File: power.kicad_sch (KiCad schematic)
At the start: 96 parts, among them Q5 NX138BKWX

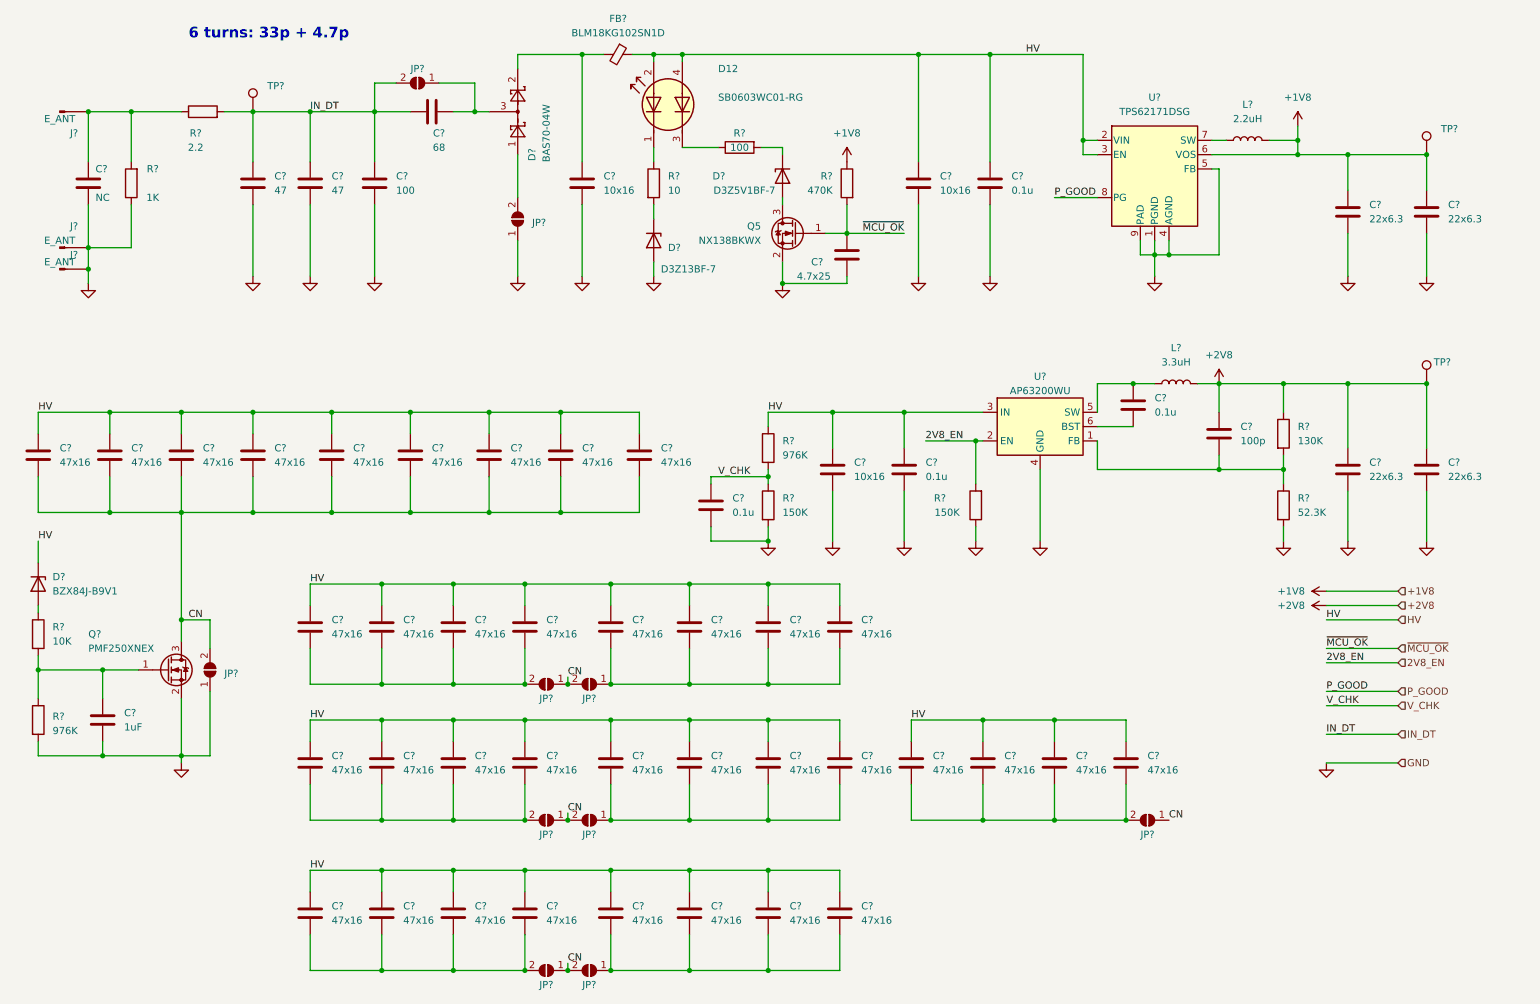
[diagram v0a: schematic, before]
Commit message: G2 revision
G2 revision = Kampela development kit

Features:
- electronics is more stable and reliable
- better power harvesting efficiency
- fixed a touchscreen instability with powerful NFC transmitters
- mechanical layout improved for low-volume productions for a devkit batch
- NFC coil placed closer to the phone antenna. The coil parameters are optimized based on a mathematical model of the NFS harvester circuit.
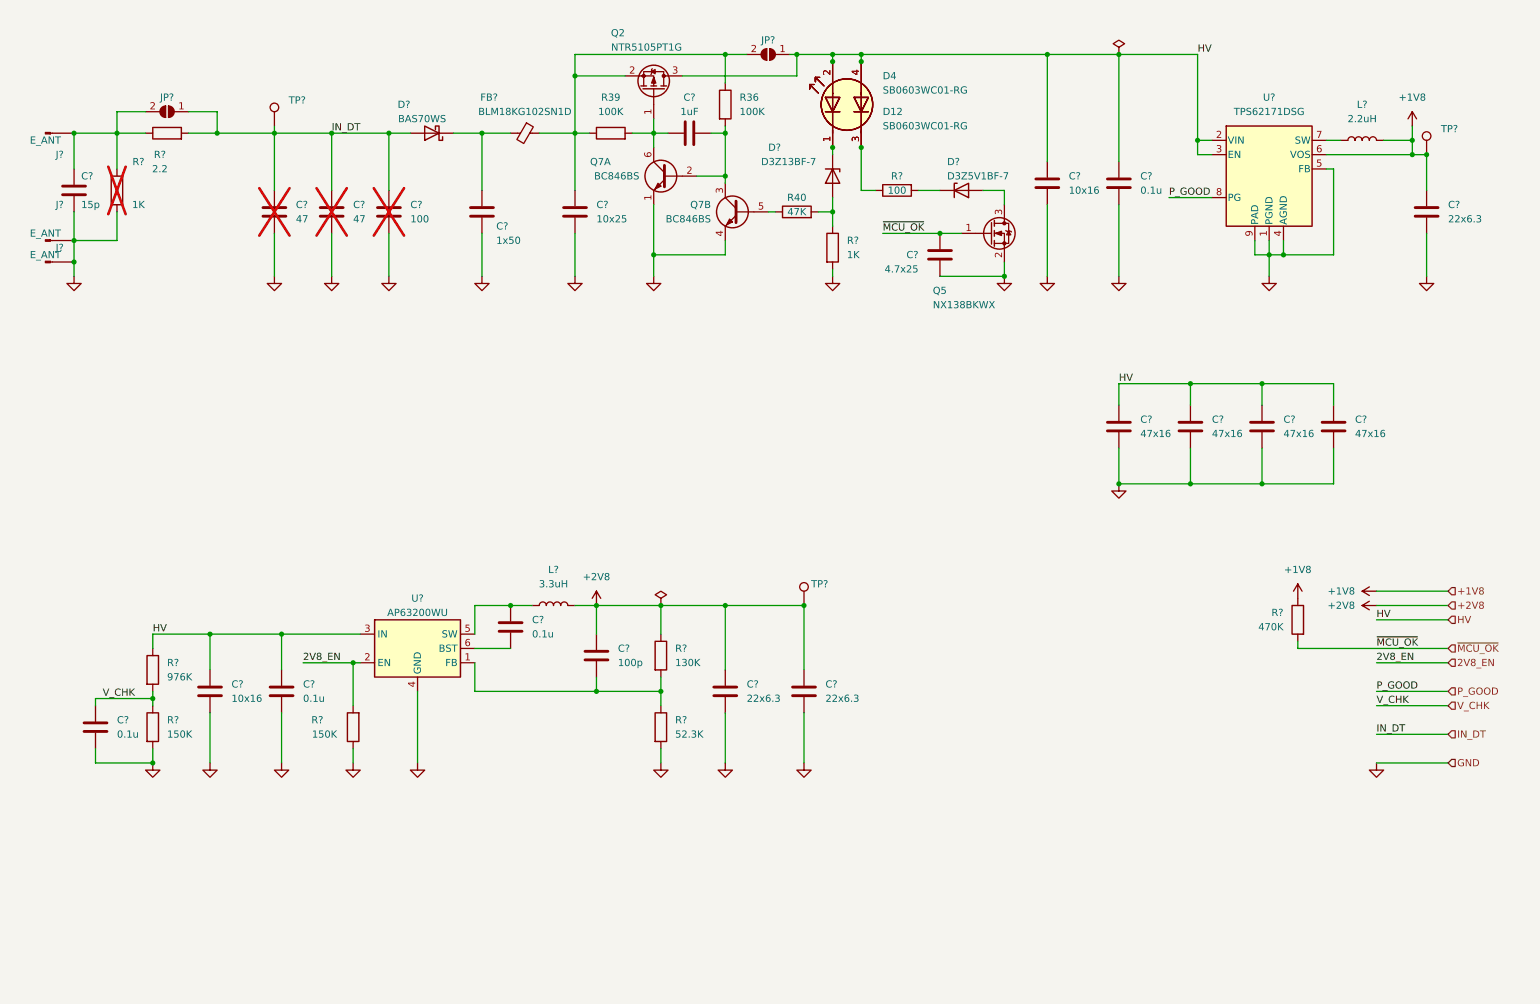
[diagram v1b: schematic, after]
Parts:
- removed C? (x33): 47x16, Capacitor_SMD:C_1210_3225Metric, symbol Device:C
- removed C?: 22x6.3, Capacitor_SMD:C_0603_1608Metric, symbol Device:C
- removed C?: 68, Capacitor_SMD:C_0603_1608Metric, symbol Device:C
- removed C?: 1uF, Capacitor_SMD:C_0402_1005Metric, symbol Device:C
- removed C?: 4.7x25, Capacitor_SMD:C_0402_1005Metric, symbol Device:C
- removed D?: D3Z5V1BF-7, Diode_SMD:D_SOD-323F, symbol Device:D_Zener
- removed D?: BZX84J-B9V1, Diode_SMD:D_SOD-323F, symbol Device:D_Zener
- removed D?: BAS70-04W, Package_TO_SOT_SMD:SOT-323_SC-70, symbol Diode:BAT54SW
- removed D?: D3Z13BF-7, Diode_SMD:D_SOD-323F, symbol Device:D_Zener
- removed FB?: BLM18KG102SN1D, Inductor_SMD:L_0603_1608Metric, symbol Device:FerriteBead_Small
- removed JP? (x10): SolderJumper_2_Open, MyLib:SolderJumper_0.8.x1mm, symbol Jumper:SolderJumper_2_Open
- removed Q?: PMF250XNEX, Package_TO_SOT_SMD:SOT-323_SC-70, symbol Device:Q_NMOS_GSD
- removed R?: 10, Resistor_SMD:R_0402_1005Metric, symbol Device:R
- removed R?: 10K, Resistor_SMD:R_0402_1005Metric, symbol Device:R
- removed R?: 976K, Resistor_SMD:R_0402_1005Metric, symbol Device:R
- removed R?: 100, Resistor_SMD:R_0402_1005Metric, symbol Device:R
- added C?: 1uF, Capacitor_SMD:C_0402_1005Metric, symbol Device:C
- added C?: 1x50, Capacitor_SMD:C_0402_1005Metric, symbol Device:C
- added C?: 4.7x25, Capacitor_SMD:C_0402_1005Metric, symbol Device:C
- added D4: SB0603WC01-RG, MyLib:LED_DUAL_0603, symbol Device:LED_Dual_KAKA
- added D?: BAS70WS, Diode_SMD:D_SOD-323F, symbol Device:D_Schottky
- added D?: D3Z5V1BF-7, Diode_SMD:D_SOD-323F, symbol Device:D_Zener
- added D?: D3Z13BF-7, Diode_SMD:D_SOD-323F, symbol Device:D_Zener
- added FB?: BLM18KG102SN1D, Inductor_SMD:L_0603_1608Metric, symbol Device:FerriteBead_Small
- added JP? (x2): SolderJumper_2_Open, MyLib:SolderJumper_0.8.x1mm, symbol Jumper:SolderJumper_2_Open
- added Q2: NTR5105PT1G, Package_TO_SOT_SMD:SOT-23, symbol Device:Q_PMOS_GSD
- added Q7: BC846BS, Package_TO_SOT_SMD:SOT-363_SC-70-6, symbol Transistor_BJT:BC846BS
- added R36, R39: 100K, Resistor_SMD:R_0402_1005Metric, symbol Device:R
- added R40: 47K, Resistor_SMD:R_0402_1005Metric, symbol Device:R
- added R?: 1K, Resistor_SMD:R_0402_1005Metric, symbol Device:R
- added R?: 100, Resistor_SMD:R_0402_1005Metric, symbol Device:R
- C?: value NC -> 15p
- C? (x3), R?: now not fitted
- C?: value 10x16 -> 10x25
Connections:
- net GND: now also C?.1, C?.1, C?.1, C?.1, C?.1, C?.2, Q7.1 (E1), Q7.4 (E2), R?.2
- net HV: now also D4.2 (K1), D4.4 (K2), JP?.1 (A), Q2.3 (D)
- net IN_DT: now also D?.2 (A), JP?.1 (A)
- net ~{MCU_OK}: now also C?.2
- net at Q5.3 (D): now also D?.2 (A)
- net at C?.1, J?.1 (Pin_1), R?.1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: now also JP?.2 (B)
- net at D12.1 (A1): now also D4.1 (A1), D?.1 (K)
- net at D12.3 (A2): now also D4.3 (A2), R?.1
- net at C?.2: now also FB?.1, JP?.2 (B), Q2.2 (S), R36.1, R39.1
- new net: C?.1, Q2.1 (G), Q7.6 (C1), R39.2
- new net: C?.2, Q7.2 (B1), Q7.3 (C2), R36.2
- new net: D?.2 (A), R40.2, R?.1
- new net: C?.1, D?.1 (K), FB?.2
- new net: D?.1 (K), R?.2
- new net: Q7.5 (B2), R40.1
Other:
- note removed: "6 turns: 33p + 4.7p"
- moved on the sheet: C?, J?, L?, R?, TP?, U?

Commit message: G5 revision
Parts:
- added TP? (x6): TestPoint, TestPoint:TestPoint_Pad_D1.0mm, symbol Connector:TestPoint
- C?: value 1uF -> 1x50
- C?: footprint Capacitor_SMD:C_0402_1005Metric -> Capacitor_SMD:C_0603_1608Metric
- D4: value SB0603WC01-RG -> 156125RG73000; footprint MyLib:LED_DUAL_0603 -> MyLib:SMD4_WL-SBRW-1205_REV-MOUNT_WRE
- renumbered Q7 to Q9, R39 to R40, R40 to R41, R36 to R42
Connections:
- net GND: now also TP?.1, TP?.1, TP?.1
- net HV: now also D4.3 (A2), TP?.1; no longer D4.2 (K1)
- net at C?.2, FB?.1, JP?.2 (B)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: now also TP?.1
- net at C?.1, J?.1 (Pin_1), JP?.2 (B)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: now also TP?.1
- net at D12.1 (A1), D?.1 (K): now also D4.2 (K2); no longer D4.1 (A1)
- net at D12.3 (A2), R?.1: now also D4.1 (K1); no longer D4.3 (A2)

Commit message: Next revision
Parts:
- removed C?: 1x50, Capacitor_SMD:C_0402_1005Metric, symbol Device:C
- removed C? (x4): 47x16, Capacitor_SMD:C_1210_3225Metric, symbol Device:C
- removed C? (x4): 0.1u, Capacitor_SMD:C_0402_1005Metric, symbol Device:C
- removed C?: 100p, Capacitor_SMD:C_0402_1005Metric, symbol Device:C
- removed C?: 100, Capacitor_SMD:C_0603_1608Metric, symbol Device:C
- removed C? (x2): 10x16, Capacitor_SMD:C_0603_1608Metric, symbol Device:C
- removed C?: 10x25, Capacitor_SMD:C_0603_1608Metric, symbol Device:C
- removed C? (x2): 22x6.3, Capacitor_SMD:C_0603_1608Metric, symbol Device:C
- removed C? (x2): 47, Capacitor_SMD:C_0603_1608Metric, symbol Device:C
- removed C?: 4.7x25, Capacitor_SMD:C_0603_1608Metric, symbol Device:C
- removed D12: SB0603WC01-RG, MyLib:LED_DUAL_0603, symbol Device:LED_Dual_KAKA
- removed D4: 156125RG73000, MyLib:SMD4_WL-SBRW-1205_REV-MOUNT_WRE, symbol Device:LED_Dual_KAKA
- removed D?: D3Z5V1BF-7, Diode_SMD:D_SOD-323F, symbol Device:D_Zener
- removed JP? (x2): SolderJumper_2_Open, MyLib:SolderJumper_0.8.x1mm, symbol Jumper:SolderJumper_2_Open
- removed L?: 3.3uH, Inductor_SMD:L_Wuerth_MAPI-3015, symbol Device:L
- removed Q5: NX138BKWX, Package_TO_SOT_SMD:SOT-323_SC-70, symbol Transistor_FET:2N7002
- removed R40, R42: 100K, Resistor_SMD:R_0402_1005Metric, symbol Device:R
- removed R41: 47K, Resistor_SMD:R_0402_1005Metric, symbol Device:R
- removed R?: 1K, Resistor_SMD:R_0603_1608Metric, symbol Device:R
- removed R?: 1K, Resistor_SMD:R_0402_1005Metric, symbol Device:R
- removed R? (x2): 150K, Resistor_SMD:R_0402_1005Metric, symbol Device:R
- removed R?: 52.3K, Resistor_SMD:R_0402_1005Metric, symbol Device:R
- removed R?: 470K, Resistor_SMD:R_0402_1005Metric, symbol Device:R
- removed R?: 976K, Resistor_SMD:R_0402_1005Metric, symbol Device:R
- removed R?: 100, Resistor_SMD:R_0402_1005Metric, symbol Device:R
- removed R?: 130K, Resistor_SMD:R_0402_1005Metric, symbol Device:R
- removed U?: AP63200WU, Package_TO_SOT_SMD:TSOT-23-6, symbol Regulator_Switching:AP63201WU
- added C10, C17, C29, C4, C7: 0.1, Capacitor_SMD:C_0201_0603Metric, symbol Device:C
- added C11, C22, C38: 22x6.3, Capacitor_SMD:C_0603_1608Metric, symbol Device:C
- added C12, C13, C15, C16, C19, C21, C23, C25, C27, C28, C30, C31, C32, C33, C34, C35, C36, C37, C6, C9: 22x16, Capacitor_SMD:C_0603_1608Metric, symbol Device:C
- added C18, C26, C8: 10x25, Capacitor_SMD:C_0603_1608Metric, symbol Device:C
- added C20: 1x50, Capacitor_SMD:C_0402_1005Metric, symbol Device:C
- added D3: RED, LED_SMD:LED_0402_1005Metric, symbol Device:LED
- added L1: 4.7uH, Inductor_SMD:L_0603_1608Metric, symbol Device:L
- added R10, R13: 100K, Resistor_SMD:R_0201_0603Metric, symbol Device:R
- added R11: 52.3K, Resistor_SMD:R_0201_0603Metric, symbol Device:R
- added R12, R15: 10K, Resistor_SMD:R_0201_0603Metric, symbol Device:R
- added R14: 46.4K, Resistor_SMD:R_0201_0603Metric, symbol Device:R
- added R7: 1M, Resistor_SMD:R_0201_0603Metric, symbol Device:R
- added R8: 150K, Resistor_SMD:R_0201_0603Metric, symbol Device:R
- added U2: NCP170AMX180TBG, Package_DFN_QFN:OnSemi_XDFN4-1EP_1.0x1.0mm_EP0.52x0.52mm, symbol Regulator_Linear:NCP115AMX250TCG
- added U3: AP62250Z6, Package_TO_SOT_SMD:SOT-563, symbol Regulator_Switching:AP62250Z6
- C?: Field5 (none) -> 0603
- C?: Size (none) -> 0402
- D?: value D3Z13BF-7 -> D3Z13BF-7
- L?: value 2.2uH -> 4.7uH; footprint Inductor_SMD:L_Wuerth_MAPI-3015 -> Inductor_SMD:L_0603_1608Metric; Size (none) -> 0603
- R?: Size (none) -> 0603
- renumbered Q9 to Q2, Q2 to Q?
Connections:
- net +1V8: now also C38.1, U3.5 (EN)
- net GND: now also C10.1, C11.1, C12.2, C13.2, C15.2, C16.2, C18.2, C19.2, C21.2, C22.2, C23.2, C25.2, C26.2, C27.2, C28.2, C29.1, C30.2, C31.2, C32.2, C33.2, C34.2, C35.2, C36.2, C37.2, C38.2, C4.1, C6.2, C7.1, C8.2, C9.2, R12.1, R15.1, R8.1, U2.2 (GND), U2.5 (GND), U3.3 (GND)
- net HV: now also C10.2, C12.1, C13.1, C15.1, C16.1, C19.1, C20.2, C21.1, C23.1, C25.1, C26.1, C27.1, C28.1, C29.2, C30.1, C31.1, C32.1, C33.1, C34.1, C35.1, C36.1, C37.1, C6.1, C8.1, C9.1, D3.2 (A), R7.2, U3.1 (VIN)
- net V_CHK: now also C4.2, R7.1, R8.2
- net at FB?.1, Q?.2 (S), TP?.1: now also C18.1, R10.1, R13.2
- net at Q2.6 (C1), Q?.1 (G): now also C20.1, R10.2
- net at Q2.2 (B1), Q2.3 (C2): now also R13.1
- net at D?.1 (K): now also D3.1 (K)
- net at D?.2 (A): now also R14.1, R15.2
- net at Q2.5 (B2): now also R14.2
- net +2V8 renamed +5V
- net +5V: now also C22.1, C7.2, L1.2, R11.2, U2.3 (EN), U2.4 (IN)
- net IN_DT renamed OUT_DT
- new net: R11.1, R12.2, U3.6 (FB)
- new net: C17.1, U3.4 (BST)
- new net: C17.2, L1.1, U3.2 (SW)
- new net +3V0: C11.2, U2.1 (OUT)
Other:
- moved on the sheet: C?, D?, FB?, J?, L?, Q2A, Q2B, Q?, R?, TP?, U?
